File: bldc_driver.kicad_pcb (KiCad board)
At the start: 2 copper layers, 5 parts, among them U1 AS5048A, U2 STM32G0B1KCTx, U3 SN65HVD230, U4 UA78M33QDCYRQ1, U5 DRV8317HREER

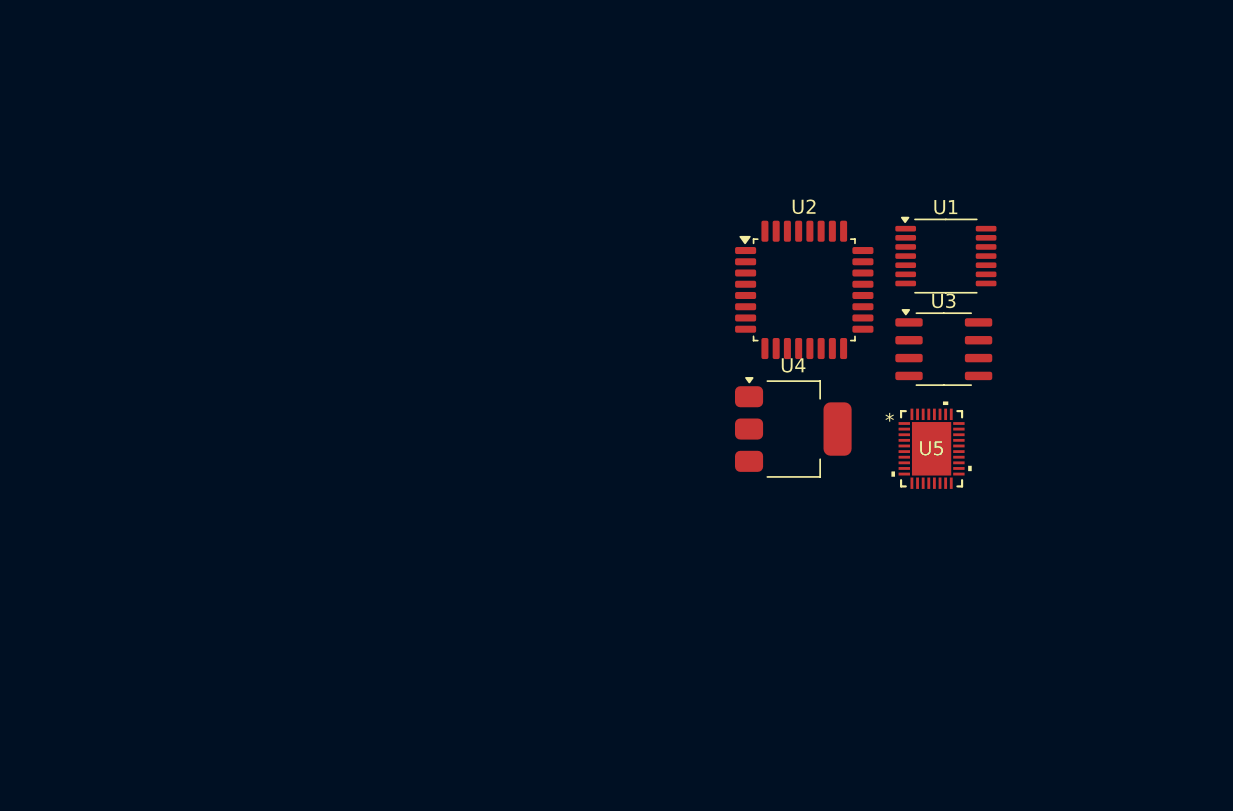
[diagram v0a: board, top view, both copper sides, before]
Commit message: initial placement of componeents
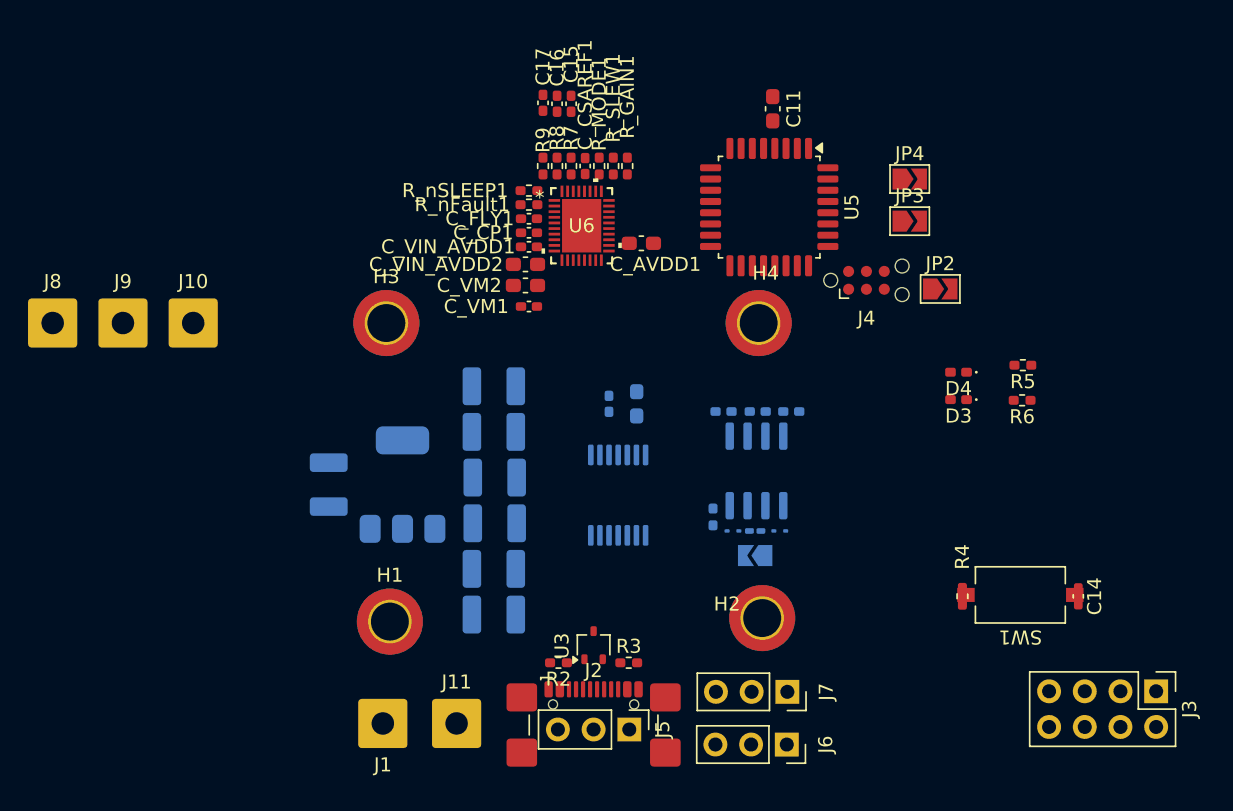
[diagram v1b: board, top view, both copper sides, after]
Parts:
- removed the U5 at (130.1, 71.7)
- added C1: 10u, Capacitor_SMD:C_1210_3225Metric_Pad1.33x2.70mm_HandSolder, B.Cu at (98.9, 83.5)
- added C10: 100n, Capacitor_SMD:C_0402_1005Metric_Pad0.74x0.62mm_HandSolder, B.Cu at (115.2, 69.0)
- added C11: 100n, Capacitor_SMD:C_0603_1608Metric_Pad1.08x0.95mm_HandSolder, F.Cu at (118.8, 47.5)
- added C12: 100n, Capacitor_SMD:C_0402_1005Metric_Pad0.74x0.62mm_HandSolder, B.Cu at (107.1, 68.5)
- added C13: 10u, Capacitor_SMD:C_0603_1608Metric_Pad1.08x0.95mm_HandSolder, B.Cu at (109.1, 68.5)
- added C14: 100n, Capacitor_SMD:C_0402_1005Metric_Pad0.74x0.62mm_HandSolder, F.Cu at (140.5, 82.2)
- added C15: 100n, Capacitor_SMD:C_0402_1005Metric_Pad0.74x0.62mm_HandSolder, F.Cu at (104.4, 47.1)
- added C16: 100n, Capacitor_SMD:C_0402_1005Metric_Pad0.74x0.62mm_HandSolder, F.Cu at (103.4, 47.1)
- added C17: 100n, Capacitor_SMD:C_0402_1005Metric_Pad0.74x0.62mm_HandSolder, F.Cu at (102.4, 47.1)
- added C2: 10u, Capacitor_SMD:C_1210_3225Metric_Pad1.33x2.70mm_HandSolder, B.Cu at (98.9, 80.2)
- added C3: 10u, Capacitor_SMD:C_1210_3225Metric_Pad1.33x2.70mm_HandSolder, B.Cu at (99.0, 77.0)
- added C4: 10u, Capacitor_SMD:C_1210_3225Metric_Pad1.33x2.70mm_HandSolder, B.Cu at (99.0, 73.8)
- added C5: 10u, Capacitor_SMD:C_1210_3225Metric_Pad1.33x2.70mm_HandSolder, B.Cu at (98.9, 70.5)
- added C6: 10u, Capacitor_SMD:C_1210_3225Metric_Pad1.33x2.70mm_HandSolder, B.Cu at (98.9, 67.2)
- added C7: 100n, Capacitor_SMD:C_0402_1005Metric_Pad0.74x0.62mm_HandSolder, B.Cu at (117.7, 69.0)
- added C8: 10u, Capacitor_SMD:C_1210_3225Metric_Pad1.33x2.70mm_HandSolder, B.Cu at (87.1, 74.2)
- added C9: 100n, Capacitor_SMD:C_0402_1005Metric_Pad0.74x0.62mm_HandSolder, B.Cu at (120.1, 69.0)
- added C_AVDD1: 2.2u, Capacitor_SMD:C_0603_1608Metric_Pad1.08x0.95mm_HandSolder, F.Cu at (109.4, 57.1)
- added C_CP1: 1u, Capacitor_SMD:C_0402_1005Metric_Pad0.74x0.62mm_HandSolder, F.Cu at (101.4, 56.3)
- added C_CSAREF1: 0.1u, Capacitor_SMD:C_0402_1005Metric_Pad0.74x0.62mm_HandSolder, F.Cu at (105.4, 51.6)
- added C_FLY1: 0.1u, Capacitor_SMD:C_0402_1005Metric_Pad0.74x0.62mm_HandSolder, F.Cu at (101.4, 55.3)
- added C_VIN_AVDD1: 0.1u, Capacitor_SMD:C_0402_1005Metric_Pad0.74x0.62mm_HandSolder, F.Cu at (101.4, 57.3)
- added C_VIN_AVDD2: 10u, Capacitor_SMD:C_0603_1608Metric_Pad1.08x0.95mm_HandSolder, F.Cu at (101.2, 58.6)
- added C_VM1: 0.1u, Capacitor_SMD:C_0402_1005Metric_Pad0.74x0.62mm_HandSolder, F.Cu at (101.4, 61.6)
- added C_VM2: 10u, Capacitor_SMD:C_0603_1608Metric_Pad1.08x0.95mm_HandSolder, F.Cu at (101.2, 60.1)
- added D1: ESD9B3.3ST5G, Diode_SMD:D_SOD-923, B.Cu at (119.2, 77.5)
- added D2: ESD9B3.3ST5G, Diode_SMD:D_SOD-923, B.Cu at (115.9, 77.5)
- added D3: LED, LED_SMD:LED_0402_1005Metric_Pad0.77x0.64mm_HandSolder, F.Cu at (132.0, 68.2)
- added D4: LED, LED_SMD:LED_0402_1005Metric_Pad0.77x0.64mm_HandSolder, F.Cu at (132.0, 66.2)
- added H1: MountingHole_Pad, MountingHole:MountingHole_2.7mm_M2.5_DIN965_Pad_TopBottom, F.Cu at (91.5, 84.0)
- added H2: MountingHole_Pad, MountingHole:MountingHole_2.7mm_M2.5_DIN965_Pad_TopBottom, F.Cu at (118.0, 83.8)
- added H3: MountingHole_Pad, MountingHole:MountingHole_2.7mm_M2.5_DIN965_Pad_TopBottom, F.Cu at (91.2, 62.8)
- added H4: MountingHole_Pad, MountingHole:MountingHole_2.7mm_M2.5_DIN965_Pad_TopBottom, F.Cu at (117.8, 62.8)
- added J1: Conn_01x01_Pin, Connector_Wire:SolderWire-0.75sqmm_1x01_D1.25mm_OD3.5mm, F.Cu at (91.0, 91.2)
- added J10: Conn_01x01_Pin, Connector_Wire:SolderWire-0.75sqmm_1x01_D1.25mm_OD3.5mm, F.Cu at (77.5, 62.8)
- added J11: Conn_01x01_Pin, Connector_Wire:SolderWire-0.75sqmm_1x01_D1.25mm_OD3.5mm, F.Cu at (96.2, 91.2)
- added J2: USB_C_Receptacle_USB2.0_16P, Connector_USB:USB_C_Receptacle_GCT_USB4110, F.Cu at (106.0, 92.5)
- added J3: Conn_01x08_Pin, Connector_PinHeader_2.54mm:PinHeader_2x04_P2.54mm_Vertical, F.Cu at (146.0, 89.0)
- added J4: Conn_ARM_SWD_TagConnect_TC2030-NL, Connector:Tag-Connect_TC2030-IDC-NL_2x03_P1.27mm_Vertical, F.Cu at (125.4, 59.7)
- added J5: Conn_01x03_Pin, Connector_PinHeader_2.54mm:PinHeader_1x03_P2.54mm_Vertical, F.Cu at (108.5, 91.7)
- added J6: Conn_01x03_Pin, Connector_PinSocket_2.54mm:PinSocket_1x03_P2.54mm_Vertical, F.Cu at (119.8, 92.8)
- added J7: Conn_01x03_Pin, Connector_PinSocket_2.54mm:PinSocket_1x03_P2.54mm_Vertical, F.Cu at (119.8, 89.0)
- added J8: Conn_01x01_Pin, Connector_Wire:SolderWire-0.75sqmm_1x01_D1.25mm_OD3.5mm, F.Cu at (67.5, 62.8)
- added J9: Conn_01x01_Pin, Connector_Wire:SolderWire-0.75sqmm_1x01_D1.25mm_OD3.5mm, F.Cu at (72.5, 62.8)
- added JP1: SolderJumper_2_Open, Jumper:SolderJumper-2_P1.3mm_Open_TrianglePad1.0x1.5mm, B.Cu at (117.5, 79.3)
- added JP2: SolderJumper_2_Open, Jumper:SolderJumper-2_P1.3mm_Open_TrianglePad1.0x1.5mm, F.Cu at (130.7, 60.3)
- added JP3: SolderJumper_2_Open, Jumper:SolderJumper-2_P1.3mm_Open_TrianglePad1.0x1.5mm, F.Cu at (128.5, 55.5)
- added JP4: SolderJumper_2_Open, Jumper:SolderJumper-2_P1.3mm_Open_TrianglePad1.0x1.5mm, F.Cu at (128.5, 52.5)
- added R1: 10k, Resistor_SMD:R_0402_1005Metric_Pad0.72x0.64mm_HandSolder, B.Cu at (114.5, 76.5)
- added R2: 5.1k, Resistor_SMD:R_0402_1005Metric_Pad0.72x0.64mm_HandSolder, F.Cu at (103.5, 86.9)
- added R3: 5.1k, Resistor_SMD:R_0402_1005Metric_Pad0.72x0.64mm_HandSolder, F.Cu at (108.5, 86.9)
- added R4: 10K, Resistor_SMD:R_0402_1005Metric_Pad0.72x0.64mm_HandSolder, F.Cu at (132.2, 82.2)
- added R5: 1k, Resistor_SMD:R_0402_1005Metric_Pad0.72x0.64mm_HandSolder, F.Cu at (136.6, 65.8)
- added R6: 1k, Resistor_SMD:R_0402_1005Metric_Pad0.72x0.64mm_HandSolder, F.Cu at (136.5, 68.2)
- added R7: 100R, Resistor_SMD:R_0402_1005Metric_Pad0.72x0.64mm_HandSolder, F.Cu at (104.4, 51.6)
- added R8: 100R, Resistor_SMD:R_0402_1005Metric_Pad0.72x0.64mm_HandSolder, F.Cu at (103.4, 51.6)
- added R9: 100R, Resistor_SMD:R_0402_1005Metric_Pad0.72x0.64mm_HandSolder, F.Cu at (102.4, 51.6)
- added R_GAIN1: 0R, Resistor_SMD:R_0402_1005Metric_Pad0.72x0.64mm_HandSolder, F.Cu at (108.4, 51.6)
- added R_MODE1: 0R, Resistor_SMD:R_0402_1005Metric_Pad0.72x0.64mm_HandSolder, F.Cu at (106.4, 51.6)
- added R_SLEW1: 0R, Resistor_SMD:R_0402_1005Metric_Pad0.72x0.64mm_HandSolder, F.Cu at (107.4, 51.6)
- added R_nFault1: 5.1k, Resistor_SMD:R_0402_1005Metric_Pad0.72x0.64mm_HandSolder, F.Cu at (101.4, 54.3)
- added R_nSLEEP1: 5.1k, Resistor_SMD:R_0402_1005Metric_Pad0.72x0.64mm_HandSolder, F.Cu at (101.4, 53.3)
- added R_term1: 120R, Resistor_SMD:R_0201_0603Metric_Pad0.64x0.40mm_HandSolder, B.Cu at (117.5, 77.5)
- added SW1: SW_Push, Button_Switch_SMD:SW_Tactile_SPST_NO_Straight_CK_PTS636Sx25SMTRLFS, F.Cu at (136.4, 82.1)
- added U1: UA78M33QDCYRQ1, Package_TO_SOT_SMD:SOT-223-3_TabPin2, B.Cu at (92.4, 74.2)
- added U2: SN65HVD230, Package_SO:SOIC-8_3.9x4.9mm_P1.27mm, B.Cu at (117.6, 73.3)
- U3: renamed from U4; value UA78M33QDCYRQ1 -> TPD2E2U06DCK; footprint Package_TO_SOT_SMD:SOT-223-3_TabPin2 -> Package_TO_SOT_SMD:SOT-323_SC-70
- U4: renamed from U2; value STM32G0B1KCTx -> AS5048A; footprint Package_QFP:LQFP-32_7x7mm_P0.8mm -> Package_SO:TSSOP-14_4.4x5mm_P0.65mm; moved to B.Cu
- U5: renamed from U3; value SN65HVD230 -> STM32G0B1KCTx; footprint Package_SO:SOIC-8_3.9x4.9mm_P1.27mm -> Package_QFP:LQFP-32_7x7mm_P0.8mm
- U6: renamed from U1; value AS5048A -> DRV8317HREER; footprint Package_SO:TSSOP-14_4.4x5mm_P0.65mm -> bldc_driver:WQFN36_REE_TEX
- moved U6 26.0 mm to (105.2, 55.8)
- moved U3 20.9 mm to (106.0, 85.7), turned to 90 degrees
- moved U4 19.7 mm to (107.8, 75.0), turned to -90 degrees
- moved U5 16.0 mm to (118.5, 54.5), turned to -90 degrees
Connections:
- U3 pad 1: unconnected-(U4-IN-Pad1) -> USB_DM
- U3 pad 2: unconnected-(U4-GND-Pad2) -> USB_DP
- U3 pad 3: unconnected-(U4-OUT-Pad3) -> GND
- U4 pad 1: unconnected-(U2-PB9-Pad1) -> SPI_NSS
- U4 pad 10: Net-(U2-PA3) -> unconnected-(U4-TEST-Pad10)
- U4 pad 11: unconnected-(U2-PA4-Pad11) -> Net-(U4-VDD3V)
- U4 pad 12: unconnected-(U2-PA5-Pad12) -> Net-(U4-VDD3V)
- U4 pad 13: Net-(U2-PA6) -> GND
- U4 pad 2: unconnected-(U2-PC14-Pad2) -> SPI_CLK
- U4 pad 3: unconnected-(U2-PC15-Pad3) -> SPI_MISO
- U4 pad 4: unconnected-(U2-VDD-Pad4) -> SPI_MOSI
- U4 pad 5: unconnected-(U2-VSS-Pad5) -> GND
- U4 pad 7: Net-(U2-PA0) -> unconnected-(U4-TEST-Pad7)
- U4 pad 9: Net-(U2-PA2) -> unconnected-(U4-TEST-Pad9)
- U5 pad 1: unconnected-(U3-D-Pad1) -> FDCAN_TX
- U5 pad 2: unconnected-(U3-GND-Pad2) -> STATUS
- U5 pad 3: unconnected-(U3-VCC-Pad3) -> ~{CAN_EN}
- U5 pad 4: unconnected-(U3-R-Pad4) -> 3V3
- U5 pad 5: unconnected-(U3-Vref-Pad5) -> GND
- U5 pad 6: unconnected-(U3-CANL-Pad6) -> nRST
- U5 pad 7: unconnected-(U3-CANH-Pad7) -> CURR_SENS_A
- U5 pad 8: unconnected-(U3-Rs-Pad8) -> CURR_SENS_B
- U6 pad 1: unconnected-(U1-~{CSn}-Pad1) -> Net-(U6-NSLEEP)
- U6 pad 10: unconnected-(U1-TEST-Pad10) -> GND
- U6 pad 11: unconnected-(U1-VDD5V-Pad11) -> MOT_A
- U6 pad 12: unconnected-(U1-VDD3V-Pad12) -> MOT_A
- U6 pad 13: unconnected-(U1-GND-Pad13) -> GND
- U6 pad 14: unconnected-(U1-PWM-Pad14) -> MOT_B
- U6 pad 2: unconnected-(U1-CLK-Pad2) -> nFAULT
- U6 pad 4: unconnected-(U1-MOSI-Pad4) -> Net-(U6-CPL)
- U6 pad 5: unconnected-(U1-TEST-Pad5) -> Net-(U6-CPH)
- U6 pad 6: unconnected-(U1-TEST-Pad6) -> Net-(U6-CP)
- U6 pad 7: unconnected-(U1-TEST-Pad7) -> VIN
- U6 pad 8: unconnected-(U1-TEST-Pad8) -> VIN
- U6 pad 9: unconnected-(U1-TEST-Pad9) -> VIN

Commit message: schematic and layout mostly done
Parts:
- removed C13: 10u, Capacitor_SMD:C_0603_1608Metric_Pad1.08x0.95mm_HandSolder
- removed JP2: SolderJumper_2_Open, Jumper:SolderJumper-2_P1.3mm_Open_TrianglePad1.0x1.5mm
- removed U4: AS5048A, Package_SO:TSSOP-14_4.4x5mm_P0.65mm
- added G***: LOGO, LOGO, B.Cu at (97.4, 75.2)
- added R10: 1k, Resistor_SMD:R_0402_1005Metric_Pad0.72x0.64mm_HandSolder, F.Cu at (101.1, 67.1)
- added R11: 1k, Resistor_SMD:R_0402_1005Metric_Pad0.72x0.64mm_HandSolder, F.Cu at (116.2, 79.1)
- added R12: 100k, Resistor_SMD:R_0402_1005Metric_Pad0.72x0.64mm_HandSolder, F.Cu at (116.2, 76.8)
- added U7: AS5047D, Package_SO:TSSOP-14_4.4x5mm_P0.65mm, B.Cu at (105.0, 73.8)
- added Y1: SiT8008xx-1x-xxE, Oscillator:Oscillator_SMD_SiT_PQFN-4Pin_2.5x2.0mm, F.Cu at (103.3, 67.1)
- C1, C10, C2, C3, C4, C5, C6, C7, C9, D1, D2, JP1, R1, R_term1, U2: moved to F.Cu
- J2: footprint Connector_USB:USB_C_Receptacle_GCT_USB4110 -> bldc_driver:USB_C_Receptacle_GCT_USB4110
- J3: value Conn_01x08_Pin -> Conn_01x03_Pin; footprint Connector_PinHeader_2.54mm:PinHeader_2x04_P2.54mm_Vertical -> Connector_PinSocket_2.54mm:PinSocket_1x03_P2.54mm_Vertical
- moved C14 54.3 mm to (88.7, 65.8), turned to 135 degrees
- moved J3 50.5 mm to (95.5, 88.8), turned to -130 degrees
- moved SW1 48.7 mm to (92.4, 61.2), turned to -135 degrees
- moved R4 44.1 mm to (91.2, 66.0), turned to -135 degrees
- moved J8 43.5 mm to (110.8, 58.0)
- moved JP4 39.2 mm to (101.6, 81.0), turned to -90 degrees
- moved JP3 38.6 mm to (99.5, 81.0), turned to -90 degrees
- moved C17 34.4 mm to (115.0, 79.1), turned to -90 degrees
- moved C16 33.6 mm to (113.8, 79.1), turned to -90 degrees
- moved D1 33.5 mm to (86.8, 69.2), turned to -90 degrees
- moved R6 33.1 mm to (106.6, 82.5)
- moved C8 33.1 mm to (120.0, 78.2), turned to 0 degrees
- moved J9 33.1 mm to (105.2, 58.0)
- moved C15 32.9 mm to (112.5, 79.0), turned to -90 degrees
- moved J6 32.9 mm to (88.6, 82.2), turned to -160 degrees
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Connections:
- net USB_DM renamed USB_D-
- net USB_DP renamed USB_D+
- C12 pad 1: Net-(U4-VDD3V) -> 3V3
- J3 pad 2: GND -> PB4
- J3 pad 3: PC6 -> PB2
- J4 pad 3: Net-(J4-~{RESET}) -> nRST
- R6 pad 1: STATUS -> Net-(D4-A)
- R6 pad 2: Net-(D4-A) -> STATUS
- R_nFault1 pad 1: AVDD_3V3 -> 3V3
- R_nSLEEP1 pad 2: AVDD_3V3 -> 3V3
- U5 pad 10: PA3 -> nFAULT
- U5 pad 17: unconnected-(U5-PB2-Pad17) -> PB2
- U5 pad 2: STATUS -> Net-(U5-PC14)
- U5 pad 20: PC6 -> STATUS
- U5 pad 26: PA15 -> VIN_SENS
- U5 pad 28: unconnected-(U5-PB4-Pad28) -> PB4
- U5 pad 3: ~{CAN_EN} -> Net-(U5-PC15)
- U5 pad 31: PB7 -> ~{CAN_EN}
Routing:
- net 3V3: track 0.00 -> 92.9 mm, vias 0 -> 7
- net GND: track 0.00 -> 85.5 mm, vias 0 -> 94
- net nRST: track 0.00 -> 38.2 mm, vias 0 -> 3
- net nFAULT: track 0.00 -> 31.7 mm, vias 0 -> 2
- net CURR_SENS_A: track 0.00 -> 24.3 mm, vias 0 -> 2
- net CURR_SENS_B: track 0.00 -> 24.1 mm, vias 0 -> 2
- net CURR_SENS_C: track 0.00 -> 23.0 mm, vias 0 -> 2
- net PB4: track 0.00 -> 22.3 mm, vias 0 -> 2
- net CAN_L: track 0.00 -> 20.0 mm
- net FDCAN_RX: track 0.00 -> 18.5 mm, vias 0 -> 2
- net PWM_A_LOW: track 0.00 -> 17.4 mm
- net VIN_SENS: track 0.00 -> 17.1 mm, vias 0 -> 2
- net CAN_H: track 0.00 -> 16.4 mm
- net VIN: track 0.00 -> 15.6 mm, vias 0 -> 5
- net PWM_A_HIGH: track 0.00 -> 15.5 mm, vias 0 -> 2
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- added copper zone on B.Cu, net GND
- added copper zone on F.Cu, net GND
- added copper zone on In1.Cu, net GND
- added copper zone on In2.Cu, net GND
- added copper zone on F.Cu, net MOT_A
- added copper zone on F.Cu, net MOT_B
- added copper zone on F.Cu, net MOT_C
- added copper zone on B.Cu, net VIN
- added copper zone on F.Cu, net VIN
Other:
- board outline added: 39.8 x 35.5 mm
- copper layers 2 -> 4
- board text added: "+"
- board text added: "-"
- board text added: "3V3"
- board text added: "6-20V"
- board text added: "A"
- board text added: "AS5047"
- board text added: "B"
- board text added: "C"
- board text added: "CAN"
- board text added: "DRV8317"
- board text added: "G"
- board text added: "H"
- board text added: "L"
- board text added: "PB2"
- board text added: "PB4"
- board text added: "RESET"
- board text added: "Rx"
- board text added: "STM32G0B1"
- board text added: "TERM"
- board text added: "TODO - check ground loops"
- board text added: "Tx"
- board text added: "U.EN"
- board text added: "UART"
- board text added: "a-osb"
- board text added: "bldc-driver"
- board text added: "v0.1"

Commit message: for review with outputs
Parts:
- removed JP3, JP4: SolderJumper_2_Open, Jumper:SolderJumper-2_P1.3mm_Open_TrianglePad1.0x1.5mm
- removed R10: 1k, Resistor_SMD:R_0402_1005Metric_Pad0.72x0.64mm_HandSolder
- C11: footprint Capacitor_SMD:C_0603_1608Metric_Pad1.08x0.95mm_HandSolder -> Capacitor_SMD:C_0402_1005Metric_Pad0.74x0.62mm_HandSolder
- C_CSAREF1, C_FLY1, C_VIN_AVDD1, C_VM1: value 0.1u -> 100n
- J3, J6, J7: footprint Connector_PinSocket_2.54mm:PinSocket_1x03_P2.54mm_Vertical -> Connector_PinHeader_2.54mm:PinHeader_1x03_P2.54mm_Vertical
- R1: value 10k -> 5.1k
- R11: value 1k -> 5.1k
- R4: value 10K -> 5.1k
- R7, R8, R9: value 100R -> 120R
- R_term1: footprint Resistor_SMD:R_0201_0603Metric_Pad0.64x0.40mm_HandSolder -> Resistor_SMD:R_0402_1005Metric_Pad0.72x0.64mm_HandSolder
- U1: value UA78M33QDCYRQ1 -> UA78M33QDCYRG4Q1
- Y1: value SiT8008xx-1x-xxE -> ECS-2520MV-160-CN; footprint Oscillator:Oscillator_SMD_SiT_PQFN-4Pin_2.5x2.0mm -> bldc_driver:Oscillator_SMD_ECS_2520MV-xxx-xx-4Pin_2.5x2.0mm
- moved D4 9.38 mm to (100.2, 82.2)
- moved R6 6.53 mm to (100.2, 81.2), turned to 0 degrees
- moved C11 1.08 mm to (100.3, 67.8), turned to 180 degrees
- moved U3 1.00 mm to (105.0, 82.8)
- moved R3 0.99 mm to (107.6, 83.6)
- moved J5 0.95 mm to (107.6, 88.9)
- moved J2 0.89 mm to (105.0, 89.2)
- moved R2 0.39 mm to (102.0, 83.6)
- moved Y1 0.25 mm to (103.1, 67.2), turned to -90 degrees
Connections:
- net Net-(U5-PC14) renamed /CLK_16MHz
- U5 pad 19: Net-(JP3-A) -> USART_TX
- U5 pad 21: Net-(JP4-A) -> USART_RX
- U5 pad 3: Net-(U5-PC15) -> unconnected-(U5-PC15-Pad3)
- Y1 pad 1: Net-(Y1-OE) -> unconnected-(Y1-Tri-State-Pad1)
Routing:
- net GND: track 85.5 -> 100.4 mm, vias 94 -> 116
- net STATUS: track 10.0 -> 3.26 mm, vias 2 -> 0
- net USART_TX: track 7.90 -> 11.9 mm
- net USART_RX: track 8.24 -> 12.2 mm
- net Net-(Y1-OE): track 3.75 -> 0.00 mm
- net Net-(JP4-A): track 2.62 -> 0.00 mm
- net Net-(JP3-A): track 2.47 -> 0.00 mm
- net Net-(U5-PC15): track 2.30 -> 0.00 mm
- net 3V3: track 92.9 -> 91.0 mm
- net Net-(D4-A): track 2.10 -> 1.01 mm
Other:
- board text removed: "TODO - check ground loops"
- board text removed: "U.EN"

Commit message: drc checked
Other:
- board text added: "MOTOR"
- board text added: "VIN"
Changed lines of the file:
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@@
 		)
 		(fp_text user "*"
-			(at -2.9845 -2 180)
+			(at -2.45 -2.7 180)
 			(unlocked yes)
 			(layer "F.SilkS")
@@
 		)
 		(fp_text user "*"
-			(at -2.9845 -2 180)
+			(at -2.45 -2.7 180)
 			(unlocked yes)
 			(layer "F.SilkS")
@@
 			(at 0 -2.38 230)
 			(layer "F.SilkS")
+			(hide yes)
 			(effects
 				(font
@@
 			(at 0 1.16 90)
 			(layer "B.SilkS")
+			(hide yes)
 			(effects
 				(font
@@
 			(at 1.325 2.175 0)
 			(layer "B.SilkS")
+			(hide yes)
 			(effects
 				(font
@@
 		)
 	)
+	(gr_text "VIN"
+		(at 111.7 86.9 32.5)
+		(layer "F.SilkS")
+		(effects
+			(font
+				(size 0.8 0.8)
+				(thickness 0.2)
+				(bold yes)
+			)
+			(justify left bottom)
+		)
+	)
 	(gr_text "6-20V"
 		(at 111.225 88.55 32.5)
@@
 		)
 	)
+	(gr_text "MOTOR"
+		(at 112.3 58.5 330)
+		(layer "F.SilkS")
+		(effects
+			(font
+				(size 1 1)
+				(thickness 0.2)
+				(bold yes)
+			)
+			(justify left bottom)
+		)
+	)
 	(gr_text "PB2\n"
-		(at 89.95 85.325 50)
+		(at 91.3 83.7 320)
 		(layer "F.SilkS")
 		(effects
@@
 	)
 	(gr_text "UART"
-		(at 102.475 87.5 0)
+		(at 103.1 87.4 0)
 		(layer "F.SilkS")
 		(effects
@@
 	)
 	(gr_text "G"
-		(at 96.05 87.575 320)
+		(at 95.9 87.4 320)
 		(layer "F.SilkS")
 		(effects
@@
 	)
 	(gr_text "PB4\n"
-		(at 94.075 85.85 320)
+		(at 93.5 85.5 320)
 		(layer "F.SilkS")
 		(effects
@@
 	)
 	(gr_text "UART"
-		(at 105.9 87.5 -0)
+		(at 107 87.4 -0)
 		(layer "B.SilkS")
 		(effects
@@
 	)
 	(gr_text "H"
-		(at 90.725 76.55 0)
+		(at 92 76.55 0)
 		(layer "B.SilkS")
 		(effects
@@
 				(bold yes)
 			)
-			(justify left bottom)
+			(justify left bottom mirror)
 		)
 	)
@@
 	)
 	(segment
-		(start 86.75 69.67)
-		(end 86.025 70.395)
+		(start 88.2 76.879232)
+		(end 88.2 79.38055)
 		(width 0.2)
 		(layer "F.Cu")
@@
 	)
 	(segment
-		(start 88.593731 78.986819)
-		(end 87.743731 79.836819)
+		(start 86.025 74.704232)
+		(end 88.2 76.879232)
 		(width 0.2)
 		(layer "F.Cu")
@@
 	)
 	(segment
-		(start 88.593731 77.682392)
-		(end 88.593731 78.986819)
+		(start 88.275 69.615)
+		(end 86.805 69.615)
 		(width 0.2)
 		(layer "F.Cu")
@@
 	)
 	(segment
-		(start 88.275 69.615)
-		(end 86.805 69.615)
+		(start 86.75 69.67)
+		(end 86.025 70.395)
 		(width 0.2)
 		(layer "F.Cu")
@@
 	)
 	(segment
-		(start 86.025 70.395)
-		(end 86.025 75.113661)
+		(start 86.805 69.615)
+		(end 86.75 69.67)
 		(width 0.2)
 		(layer "F.Cu")
@@
 	)
 	(segment
-		(start 86.025 75.113661)
-		(end 88.593731 77.682392)
+		(start 86.025 70.395)
+		(end 86.025 74.704232)
 		(width 0.2)
 		(layer "F.Cu")
@@
 	)
 	(segment
-		(start 86.805 69.615)
-		(end 86.75 69.67)
+		(start 88.2 79.38055)
+		(end 87.743731 79.836819)
 		(width 0.2)
 		(layer "F.Cu")
@@
 	)
 	(segment
-		(start 102 86.775)
-		(end 102 82.708869)
+		(start 104.2 87)
+		(end 104.2 88.025)
+		(width 0.2)
+		(layer "B.Cu")
+		(net 8)
+	)
+	(segment
+		(start 102 82.708869)
+		(end 102 84.8)
 		(width 0.2)
 		(layer "B.Cu")
@@
 	)
 	(segment
-		(start 104.46 88.885)
-		(end 102.35 86.775)
+		(start 102 84.8)
+		(end 104.2 87)
+		(width 0.2)
+		(layer "B.Cu")
+		(net 8)
+	)
+	(segment
+		(start 104.2 88.025)
+		(end 105.06 88.885)
 		(width 0.2)
 		(layer "B.Cu")
@@
 	)
 	(segment
-		(start 100.25 84.25)
-		(end 99.6 83.6)
+		(start 100.6 86.680761)
+		(end 100.6 84.6)
 		(width 0.2)
 		(layer "B.Cu")
@@
 	)
 	(segment
-		(start 101.25 87.685)
-		(end 101.25 87.330761)
+		(start 100.6 84.6)
+		(end 99.6 83.6)
 		(width 0.2)
 		(layer "B.Cu")
@@
 	)
 	(segment
-		(start 100.6 86.680761)
-		(end 100.6 84.25)
+		(start 101.92 88.355)
+		(end 101.92 88.000761)
 		(width 0.2)
 		(layer "B.Cu")
@@
 	)
 	(segment
-		(start 101.25 87.330761)
+		(start 101.92 88.000761)
 		(end 100.6 86.680761)
 		(width 0.2)
 		(layer "B.Cu")
-		(net 9)
-	)
-	(segment
-		(start 101.92 88.355)
-		(end 101.25 87.685)
-		(width 0.2)
-		(layer "B.Cu")

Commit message: cut rev 0.1
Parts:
- C_VIN_AVDD2, C_VM2: footprint Capacitor_SMD:C_0603_1608Metric_Pad1.08x0.95mm_HandSolder -> Capacitor_SMD:C_0805_2012Metric_Pad1.18x1.45mm_HandSolder
- SW1: footprint Button_Switch_SMD:SW_Tactile_SPST_NO_Straight_CK_PTS636Sx25SMTRLFS -> Button_Switch_SMD:SW_Push_1P1T_NO_CK_KMR2
- moved C_AVDD1 1.04 mm to (107.4, 70.8), turned to -45 degrees
- moved C_VM1 0.83 mm to (107.8, 69.5), turned to 135 degrees
- moved C_VM2 0.31 mm to (114.8, 68.7)
- moved C_VIN_AVDD2 0.25 mm to (116.5, 68.8)
- moved SW1 0.14 mm to (92.5, 61.3), turned to 45 degrees
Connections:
- J3 pad 2: PB4 -> PB2
- J3 pad 3: PB2 -> PB4
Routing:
- net GND: track 100.4 -> 124.2 mm, vias 116 -> 128
- net nRST: track 38.2 -> 43.8 mm
- net PWM_A_LOW: track 17.4 -> 14.2 mm, vias 0 -> 2
- net FDCAN_RX: track 18.5 -> 15.3 mm
- net nFAULT: track 31.7 -> 33.7 mm
- net PB4: track 22.3 -> 20.6 mm
- net PB2: track 11.5 -> 12.9 mm
- net CURR_SENS_C: track 23.0 -> 24.0 mm
- net PWM_A_HIGH: track 15.5 -> 14.8 mm
- net VIN: track 15.6 -> 15.0 mm
